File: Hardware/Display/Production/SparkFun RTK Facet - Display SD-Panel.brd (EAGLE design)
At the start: 119.6 x 193.8 mm, 662 parts, among them J1 FPC_12_0.5MM_BACKFLIP, J10 MICRO-SD-PUSH-PUSH-EXT-PIN, J11 FPC_12_0.5MM_BACKFLIP, J12 MICRO-SD-PUSH-PUSH-EXT-PIN, J13 FPC_12_0.5MM_BACKFLIP, J14 MICRO-SD-PUSH-PUSH-EXT-PIN, J15 FPC_12_0.5MM_BACKFLIP, J16 MICRO-SD-PUSH-PUSH-EXT-PIN, J17 FPC_12_0.5MM_BACKFLIP, J18 MICRO-SD-PUSH-PUSH-EXT-PIN, J19 FPC_12_0.5MM_BACKFLIP, J2 MICRO-SD-PUSH-PUSH-EXT-PIN, J20 MICRO-SD-PUSH-PUSH-EXT-PIN, J21 FPC_12_0.5MM_BACKFLIP, J22 MICRO-SD-PUSH-PUSH-EXT-PIN, J23 FPC_12_0.5MM_BACKFLIP, J24 MICRO-SD-PUSH-PUSH-EXT-PIN, J25 FPC_12_0.5MM_BACKFLIP, J26 MICRO-SD-PUSH-PUSH-EXT-PIN, J27 FPC_12_0.5MM_BACKFLIP, J28 MICRO-SD-PUSH-PUSH-EXT-PIN, J29 FPC_12_0.5MM_BACKFLIP, J3 FPC_12_0.5MM_BACKFLIP, J30 MICRO-SD-PUSH-PUSH-EXT-PIN, J31 FPC_12_0.5MM_BACKFLIP, J32 MICRO-SD-PUSH-PUSH-EXT-PIN, J4 MICRO-SD-PUSH-PUSH-EXT-PIN, J5 FPC_12_0.5MM_BACKFLIP, J6 MICRO-SD-PUSH-PUSH-EXT-PIN, J7 FPC_12_0.5MM_BACKFLIP, J8 MICRO-SD-PUSH-PUSH-EXT-PIN, J9 FPC_12_0.5MM_BACKFLIP, U1 LIS2DH12, U10 LIS2DH12, U11 LIS2DH12, U12 LIS2DH12, U13 LIS2DH12, U14 LIS2DH12, U15 LIS2DH12, U16 LIS2DH12, U2 LIS2DH12, U3 LIS2DH12, U4 LIS2DH12, U5 LIS2DH12, U6 LIS2DH12, U7 LIS2DH12, U8 LIS2DH12, U9 LIS2DH12

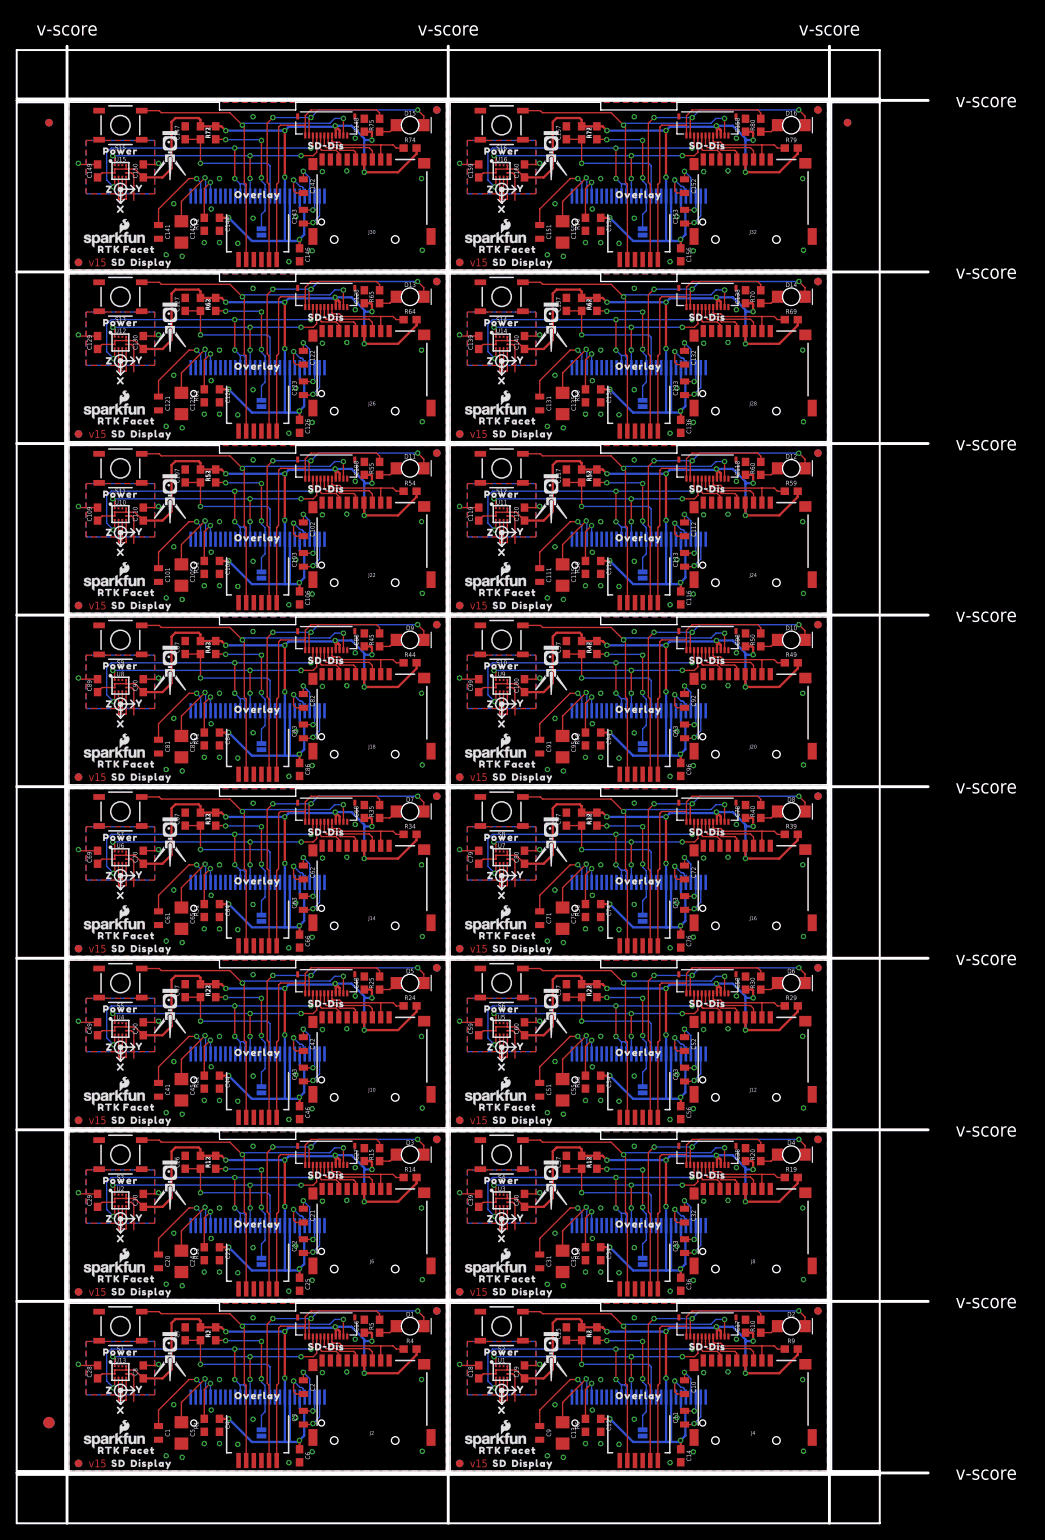
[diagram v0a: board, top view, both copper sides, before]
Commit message: Add I2C test header to display board - v1.6
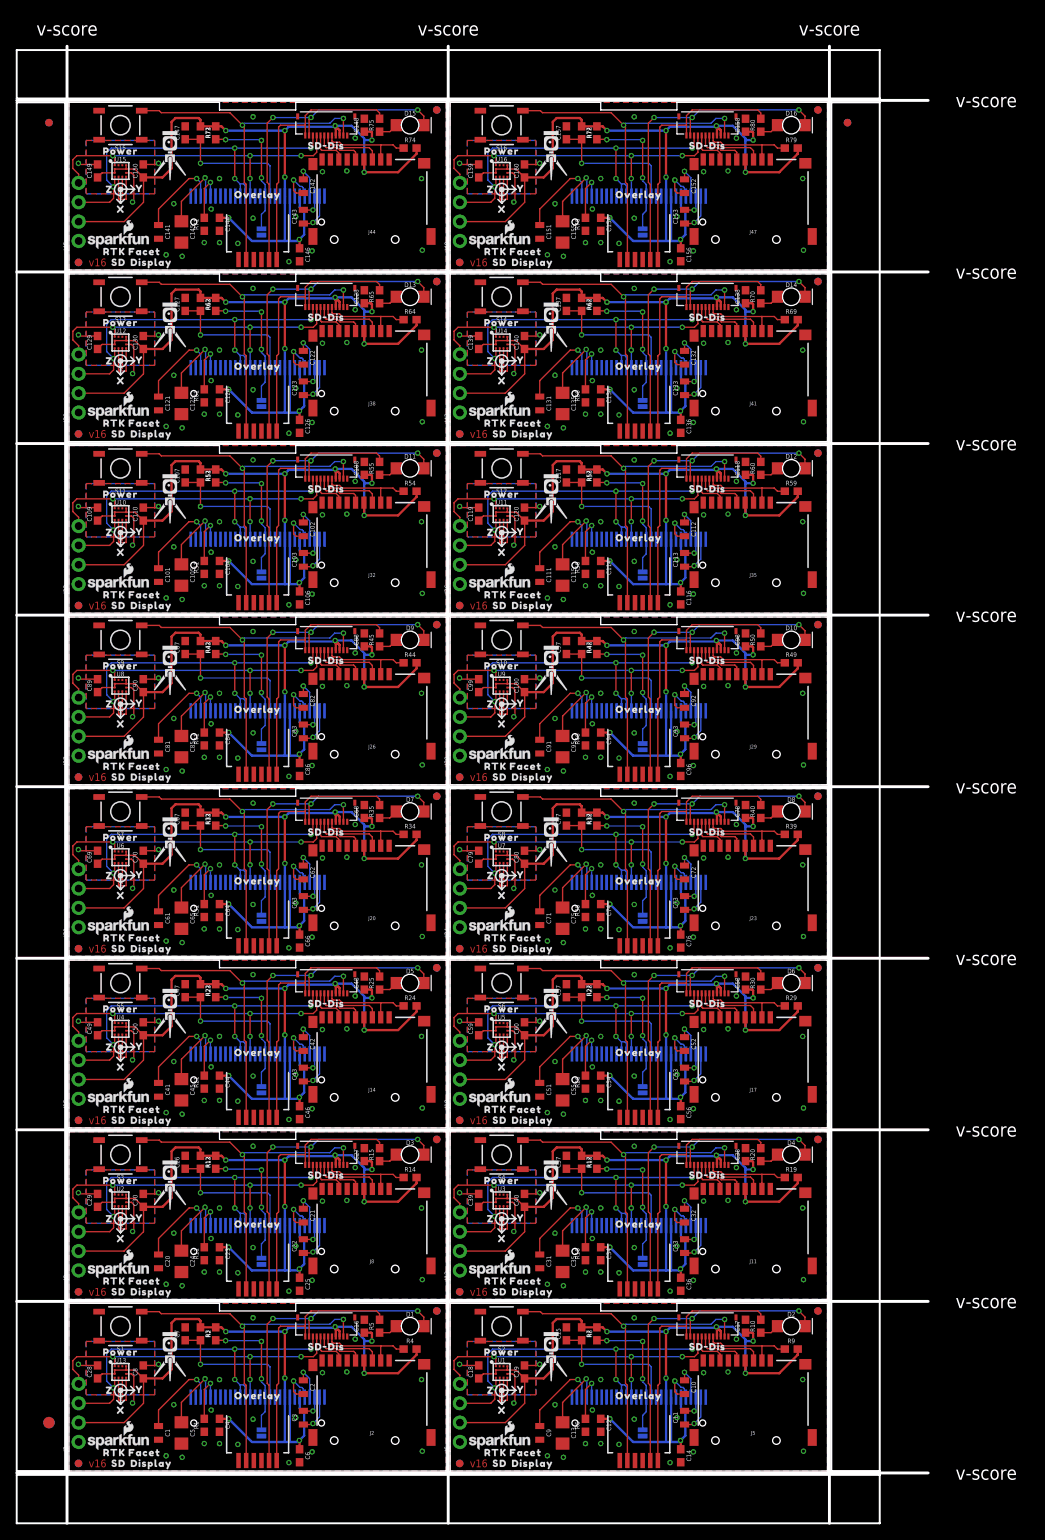
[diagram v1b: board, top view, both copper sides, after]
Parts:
- added J33, J36, J39, J42, J45, J48: (no value), SparkFun-Connectors:1X04_NO_SILK
- added J34, J37, J40, J43, J46: FPC_12_0.5MM_BACKFLIP, RTK Facet:FPC_12_DOUBLESIDED_BACKFLIP
- added J35, J38, J41, J44, J47: MICRO-SD-PUSH-PUSH-EXT-PIN, SparkFun-Connectors:MICROSD-EXTERNALPIN
- added U$193, U$209, U$225, U$241: (no value), output:DISPLAY0
- added U$194, U$210, U$226, U$242: (no value), output:SD1
- added U$195, U$211, U$227, U$243: (no value), output:#ADR#0
- added U$196, U$212, U$228, U$244: (no value), output:SD#DIS0
- added U$197, U$213, U$229, U$245: (no value), output:CHARGE0
- added U$198, U$214, U$230, U$246: (no value), output:OVERLAY0
- added U$199, U$215, U$231, U$247: (no value), output:POWER0
- added U$200, U$216, U$232, U$248: (no value), output:X0
- added U$201, U$217, U$233, U$249: (no value), output:Y1
- added U$202, U$218, U$234, U$250: (no value), output:Z2
- added U$203, U$219, U$235, U$251: (no value), output:RTK_FACET0
- added U$204, U$220, U$236, U$252: (no value), output:RTK5#SVG0
- added U$205, U$221, U$237, U$253: (no value), output:3V33
- added U$206, U$222, U$238, U$254: (no value), output:GND2
- added U$207, U$223, U$239, U$255: (no value), output:SCL0
- added U$208, U$224, U$240, U$256: (no value), output:SDA1
- J10, J16, J22, J28, J4: value MICRO-SD-PUSH-PUSH-EXT-PIN -> FPC_12_0.5MM_BACKFLIP; device SparkFun-Connectors:MICROSD-EXTERNALPIN -> RTK Facet:FPC_12_DOUBLESIDED_BACKFLIP
- J11, J17, J23, J29, J5: value FPC_12_0.5MM_BACKFLIP -> MICRO-SD-PUSH-PUSH-EXT-PIN; device RTK Facet:FPC_12_DOUBLESIDED_BACKFLIP -> SparkFun-Connectors:MICROSD-EXTERNALPIN
- J12, J18, J24, J30, J6: value MICRO-SD-PUSH-PUSH-EXT-PIN -> (none); device SparkFun-Connectors:MICROSD-EXTERNALPIN -> SparkFun-Connectors:1X04_NO_SILK
- J15, J21, J27, J3, J9: value FPC_12_0.5MM_BACKFLIP -> (none); device RTK Facet:FPC_12_DOUBLESIDED_BACKFLIP -> SparkFun-Connectors:1X04_NO_SILK
- U$109, U$157, U$61: device output:DISPLAY0 -> output:3V33
- U$110, U$158, U$62: device output:SD1 -> output:GND2
- U$111, U$159, U$63: device output:#ADR#0 -> output:SCL0
- U$112, U$160, U$64: device output:SD#DIS0 -> output:SDA1
- U$113, U$161, U$65: device output:CHARGE0 -> output:DISPLAY0
- U$114, U$162, U$18, U$66: device output:OVERLAY0 -> output:SD1
- U$115, U$163, U$19, U$67: device output:POWER0 -> output:#ADR#0
- U$116, U$164, U$20, U$68: device output:X0 -> output:SD#DIS0
- U$117, U$165, U$21, U$69: device output:Y1 -> output:CHARGE0
- U$118, U$166, U$22, U$70: device output:Z2 -> output:OVERLAY0
- U$119, U$167, U$23, U$71: device output:RTK_FACET0 -> output:POWER0
- U$120, U$168, U$24, U$72: device output:RTK5#SVG0 -> output:X0
- U$121, U$169, U$25, U$73: device output:DISPLAY0 -> output:Y1
- U$122, U$170, U$26, U$74: device output:SD1 -> output:Z2
- U$123, U$171, U$27, U$75: device output:#ADR#0 -> output:RTK_FACET0
- U$124, U$172, U$28, U$76: device output:SD#DIS0 -> output:RTK5#SVG0
- U$125, U$173, U$29, U$77: device output:CHARGE0 -> output:3V33
- U$126, U$174, U$30, U$78: device output:OVERLAY0 -> output:GND2
- U$127, U$175, U$31, U$79: device output:POWER0 -> output:SCL0
- U$128, U$176, U$32, U$80: device output:X0 -> output:SDA1
- U$129, U$177, U$33, U$81: device output:Y1 -> output:DISPLAY0
- U$130, U$178, U$34, U$82: device output:Z2 -> output:SD1
- U$131, U$179, U$35, U$83: device output:RTK_FACET0 -> output:#ADR#0
- U$132, U$180, U$36, U$84: device output:RTK5#SVG0 -> output:SD#DIS0
- U$133, U$181, U$37, U$85: device output:DISPLAY0 -> output:CHARGE0
- U$134, U$182, U$38, U$86: device output:SD1 -> output:OVERLAY0
- U$135, U$183, U$39, U$87: device output:#ADR#0 -> output:POWER0
- U$136, U$184, U$40, U$88: device output:SD#DIS0 -> output:X0
- U$137, U$185, U$41, U$89: device output:CHARGE0 -> output:Y1
- U$138, U$186, U$42, U$90: device output:OVERLAY0 -> output:Z2
- U$139, U$187, U$43, U$91: device output:POWER0 -> output:RTK_FACET0
- U$14: device output:SD1 -> output:3V33
- U$140, U$188, U$44, U$92: device output:X0 -> output:RTK5#SVG0
- U$141, U$189, U$45, U$93: device output:Y1 -> output:3V33
- U$142, U$190, U$46, U$94: device output:Z2 -> output:GND2
- U$143, U$191, U$47, U$95: device output:RTK_FACET0 -> output:SCL0
- U$144, U$192, U$48, U$96: device output:RTK5#SVG0 -> output:SDA1
- U$15: device output:#ADR#0 -> output:GND2
- U$16: device output:SD#DIS0 -> output:SCL0
- U$17: device output:CHARGE0 -> output:SDA1
- moved J27 102.1 mm to (1.27, 93.8), turned to 90 degrees
- moved J29 99.7 mm to (89.8, 94.0), turned to 0 degrees
- moved U$161 92.4 mm to (10.8, 113.5), flipped to the top
- moved U$17 91.3 mm to (3.81, 8.89)
- moved J15 90.7 mm to (1.27, 48.8), turned to 90 degrees
- moved U$137 90.2 mm to (9.25, 100.7), flipped to the top
- moved U$41 85.7 mm to (9.25, 33.2), flipped to the top
- moved U$65 85.5 mm to (10.8, 46.0), flipped to the top
- moved U$112 85.4 mm to (3.81, 76.4), flipped to the bottom
- moved J3 83.9 mm to (1.27, 3.81), turned to 90 degrees
- moved U$136 83.0 mm to (6.65, 98.0), turned to 180 degrees
- moved U$180 83.0 mm to (83.8, 128.8)
- moved U$179 82.6 mm to (78.3, 117.5), flipped to the bottom
- moved J17 82.1 mm to (89.8, 49.0), turned to 0 degrees
- moved U$16 80.1 mm to (3.81, 11.4), flipped to the bottom
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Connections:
- net 3.3V: now also J3.2
- net 3.3V1: now also J4.3, J5.4, J6.2; no longer J3.3, J3.4
- net 3.3V10: now also J31.3, J31.4, J32.4, J33.2; no longer J21.3, J21.4, J22.4
- net 3.3V11: now also J34.3, J34.4, J35.4, J36.2; no longer J23.3, J23.4, J24.4
- net 3.3V12: now also J37.3, J37.4, J38.4, J39.2; no longer J25.3, J25.4, J26.4
- net 3.3V13: now also J40.3, J40.4, J41.4, J42.2; no longer J27.3, J27.4, J28.4
- net 3.3V14: now also J43.3, J43.4, J44.4, J45.2; no longer J29.3, J29.4, J30.4
- net 3.3V15: now also J46.3, J46.4, J47.4, J48.2; no longer J31.3, J31.4, J32.4
- net 3.3V2: now also J7.3, J7.4, J8.4, J9.2; no longer J5.3, J5.4, J6.4
- net 3.3V3: now also J10.3, J10.4, J11.4, J12.2; no longer J7.3, J7.4, J8.4
- net 3.3V4: now also J13.3, J13.4, J14.4, J15.2; no longer J10.4, J9.3, J9.4
- net 3.3V5: now also J16.3, J16.4, J17.4, J18.2; no longer J11.3, J11.4, J12.4
- net 3.3V6: now also J19.3, J19.4, J20.4, J21.2; no longer J13.3, J13.4, J14.4
- net 3.3V7: now also J22.3, J22.4, J23.4, J24.2; no longer J15.3, J15.4, J16.4
- net 3.3V8: now also J25.3, J25.4, J26.4, J27.2; no longer J17.3, J17.4, J18.4
- net 3.3V9: now also J28.3, J28.4, J29.4, J30.2; no longer J19.3, J19.4, J20.4
- net CHARGE_LED1: now also J4.11; no longer J3.11
- net CHARGE_LED10: now also J31.11; no longer J21.11
- net CHARGE_LED11: now also J34.11; no longer J23.11
- net CHARGE_LED12: now also J37.11; no longer J25.11
- net CHARGE_LED13: now also J40.11; no longer J27.11
- net CHARGE_LED14: now also J43.11; no longer J29.11
- net CHARGE_LED15: now also J46.11; no longer J31.11
- net CHARGE_LED2: now also J7.11; no longer J5.11
- net CHARGE_LED3: now also J10.11; no longer J7.11
- net CHARGE_LED4: now also J13.11; no longer J9.11
- net CHARGE_LED5: now also J16.11; no longer J11.11
- net CHARGE_LED6: now also J19.11; no longer J13.11
- net CHARGE_LED7: now also J22.11; no longer J15.11
- net CHARGE_LED8: now also J25.11; no longer J17.11
- net CHARGE_LED9: now also J28.11; no longer J19.11
- net ESP_21/SDA: now also J3.3
- net ESP_21/SDA1: now also J4.10, J6.3; no longer J3.10
- net ESP_21/SDA10: now also J31.10, J33.3; no longer J21.10
- net ESP_21/SDA11: now also J34.10, J36.3; no longer J23.10
- net ESP_21/SDA12: now also J37.10, J39.3; no longer J25.10
- net ESP_21/SDA13: now also J40.10, J42.3; no longer J27.10
- net ESP_21/SDA14: now also J43.10, J45.3; no longer J29.10
- net ESP_21/SDA15: now also J46.10, J48.3; no longer J31.10
- net ESP_21/SDA2: now also J7.10, J9.3; no longer J5.10
- net ESP_21/SDA3: now also J10.10, J12.3; no longer J7.10
- net ESP_21/SDA4: now also J13.10, J15.3; no longer J9.10
- net ESP_21/SDA5: now also J16.10, J18.3; no longer J11.10
- net ESP_21/SDA6: now also J19.10, J21.3; no longer J13.10
- net ESP_21/SDA7: now also J22.10, J24.3; no longer J15.10
- net ESP_21/SDA8: now also J25.10, J27.3; no longer J17.10
- net ESP_21/SDA9: now also J28.10, J30.3; no longer J19.10
- net ESP_22/SCL: now also J3.4
- net ESP_22/SCL1: now also J4.9, J6.4; no longer J3.9
- net ESP_22/SCL10: now also J31.9, J33.4; no longer J21.9
- net ESP_22/SCL11: now also J34.9, J36.4; no longer J23.9
- net ESP_22/SCL12: now also J37.9, J39.4; no longer J25.9
- net ESP_22/SCL13: now also J40.9, J42.4; no longer J27.9
- net ESP_22/SCL14: now also J43.9, J45.4; no longer J29.9
- net ESP_22/SCL15: now also J46.9, J48.4; no longer J31.9
- net ESP_22/SCL2: now also J7.9, J9.4; no longer J5.9
- net ESP_22/SCL3: now also J10.9, J12.4; no longer J7.9
- net ESP_22/SCL4: now also J13.9, J15.4; no longer J9.9
- net ESP_22/SCL5: now also J16.9, J18.4; no longer J11.9
- net ESP_22/SCL6: now also J19.9, J21.4; no longer J13.9
- net ESP_22/SCL7: now also J22.9, J24.4; no longer J15.9
- net ESP_22/SCL8: now also J25.9, J27.4; no longer J17.9
- net ESP_22/SCL9: now also J28.9, J30.4; no longer J19.9
- net GND: now also J3.1
- net GND1: now also J4.1, J5.10, J5.11, J5.12, J5.13, J5.6, J5.9, J6.1; no longer J3.1, J4.10, J4.11, J4.12, J4.13, J4.6, J4.9
- net GND10: now also J31.1, J32.10, J32.11, J32.12, J32.13, J32.6, J32.9, J33.1; no longer J21.1, J22.10, J22.11, J22.12, J22.13, J22.6, J22.9
- net GND11: now also J34.1, J35.10, J35.11, J35.12, J35.13, J35.6, J35.9, J36.1; no longer J23.1, J24.10, J24.11, J24.12, J24.13, J24.6, J24.9
- net GND12: now also J37.1, J38.10, J38.11, J38.12, J38.13, J38.6, J38.9, J39.1; no longer J25.1, J26.10, J26.11, J26.12, J26.13, J26.6, J26.9
- net GND13: now also J40.1, J41.10, J41.11, J41.12, J41.13, J41.6, J41.9, J42.1; no longer J27.1, J28.10, J28.11, J28.12, J28.13, J28.6, J28.9
- net GND14: now also J43.1, J44.10, J44.11, J44.12, J44.13, J44.6, J44.9, J45.1; no longer J29.1, J30.10, J30.11, J30.12, J30.13, J30.6, J30.9
- net GND15: now also J46.1, J47.10, J47.11, J47.12, J47.13, J47.6, J47.9, J48.1; no longer J31.1, J32.10, J32.11, J32.12, J32.13, J32.6, J32.9
- net GND2: now also J7.1, J8.10, J8.11, J8.12, J8.13, J8.6, J8.9, J9.1; no longer J5.1, J6.10, J6.11, J6.12, J6.13, J6.6, J6.9
- net GND3: now also J10.1, J11.10, J11.11, J11.12, J11.13, J11.6, J11.9, J12.1; no longer J7.1, J8.10, J8.11, J8.12, J8.13, J8.6, J8.9
- net GND4: now also J13.1, J14.10, J14.11, J14.12, J14.13, J14.6, J14.9, J15.1; no longer J10.10, J10.11, J10.12, J10.13, J10.6, J10.9, J9.1
- net GND5: now also J16.1, J17.10, J17.11, J17.12, J17.13, J17.6, J17.9, J18.1; no longer J11.1, J12.10, J12.11, J12.12, J12.13, J12.6, J12.9
- net GND6: now also J19.1, J20.10, J20.11, J20.12, J20.13, J20.6, J20.9, J21.1; no longer J13.1, J14.10, J14.11, J14.12, J14.13, J14.6, J14.9
- net GND7: now also J22.1, J23.10, J23.11, J23.12, J23.13, J23.6, J23.9, J24.1; no longer J15.1, J16.10, J16.11, J16.12, J16.13, J16.6, J16.9
- net GND8: now also J25.1, J26.10, J26.11, J26.12, J26.13, J26.6, J26.9, J27.1; no longer J17.1, J18.10, J18.11, J18.12, J18.13, J18.6, J18.9
- net GND9: now also J28.1, J29.10, J29.11, J29.12, J29.13, J29.6, J29.9, J30.1; no longer J19.1, J20.10, J20.11, J20.12, J20.13, J20.6, J20.9
- net POWER_BTN1: now also J4.2; no longer J3.2
- net POWER_BTN10: now also J31.2; no longer J21.2
- net POWER_BTN11: now also J34.2; no longer J23.2
- net POWER_BTN12: now also J37.2; no longer J25.2
- net POWER_BTN13: now also J40.2; no longer J27.2
- net POWER_BTN14: now also J43.2; no longer J29.2
- net POWER_BTN15: now also J46.2; no longer J31.2
- net POWER_BTN2: now also J7.2; no longer J5.2
- net POWER_BTN3: now also J10.2; no longer J7.2
- net POWER_BTN4: now also J13.2; no longer J9.2
- net POWER_BTN5: now also J16.2; no longer J11.2
- net POWER_BTN6: now also J19.2; no longer J13.2
- net POWER_BTN7: now also J22.2; no longer J15.2
- net POWER_BTN8: now also J25.2; no longer J17.2
- net POWER_BTN9: now also J28.2; no longer J19.2
- net SD_!CS!1: now also J4.5, J5.2; no longer J3.5, J4.2
- net SD_!CS!10: now also J31.5, J32.2; no longer J21.5, J22.2
- net SD_!CS!11: now also J34.5, J35.2; no longer J23.5, J24.2
- net SD_!CS!12: now also J37.5, J38.2; no longer J25.5, J26.2
- net SD_!CS!13: now also J40.5, J41.2; no longer J27.5, J28.2
- net SD_!CS!14: now also J43.5, J44.2; no longer J29.5, J30.2
- net SD_!CS!15: now also J46.5, J47.2; no longer J31.5, J32.2
- net SD_!CS!2: now also J7.5, J8.2; no longer J5.5, J6.2
- net SD_!CS!3: now also J10.5, J11.2; no longer J7.5, J8.2
- net SD_!CS!4: now also J13.5, J14.2; no longer J10.2, J9.5
- net SD_!CS!5: now also J16.5, J17.2; no longer J11.5, J12.2
- net SD_!CS!6: now also J19.5, J20.2; no longer J13.5, J14.2
- net SD_!CS!7: now also J22.5, J23.2; no longer J15.5, J16.2
- net SD_!CS!8: now also J25.5, J26.2; no longer J17.5, J18.2
- net SD_!CS!9: now also J28.5, J29.2; no longer J19.5, J20.2
- net SD_CIPO1: now also J4.8, J5.7; no longer J3.8, J4.7
- net SD_CIPO10: now also J31.8, J32.7; no longer J21.8, J22.7
- net SD_CIPO11: now also J34.8, J35.7; no longer J23.8, J24.7
- net SD_CIPO12: now also J37.8, J38.7; no longer J25.8, J26.7
- net SD_CIPO13: now also J40.8, J41.7; no longer J27.8, J28.7
- net SD_CIPO14: now also J43.8, J44.7; no longer J29.8, J30.7
- net SD_CIPO15: now also J46.8, J47.7; no longer J31.8, J32.7
- net SD_CIPO2: now also J7.8, J8.7; no longer J5.8, J6.7
- net SD_CIPO3: now also J10.8, J11.7; no longer J7.8, J8.7
- net SD_CIPO4: now also J13.8, J14.7; no longer J10.7, J9.8
- net SD_CIPO5: now also J16.8, J17.7; no longer J11.8, J12.7
- net SD_CIPO6: now also J19.8, J20.7; no longer J13.8, J14.7
- net SD_CIPO7: now also J22.8, J23.7; no longer J15.8, J16.7
- net SD_CIPO8: now also J25.8, J26.7; no longer J17.8, J18.7
- net SD_CIPO9: now also J28.8, J29.7; no longer J19.8, J20.7
- net SD_COPI1: now also J4.6, J5.3; no longer J3.6, J4.3
- net SD_COPI10: now also J31.6, J32.3; no longer J21.6, J22.3
- net SD_COPI11: now also J34.6, J35.3; no longer J23.6, J24.3
- net SD_COPI12: now also J37.6, J38.3; no longer J25.6, J26.3
- net SD_COPI13: now also J40.6, J41.3; no longer J27.6, J28.3
- net SD_COPI14: now also J43.6, J44.3; no longer J29.6, J30.3
- net SD_COPI15: now also J46.6, J47.3; no longer J31.6, J32.3
- net SD_COPI2: now also J7.6, J8.3; no longer J5.6, J6.3
- net SD_COPI3: now also J10.6, J11.3; no longer J7.6, J8.3
- net SD_COPI4: now also J13.6, J14.3; no longer J10.3, J9.6
- net SD_COPI5: now also J16.6, J17.3; no longer J11.6, J12.3
- net SD_COPI6: now also J19.6, J20.3; no longer J13.6, J14.3
- net SD_COPI7: now also J22.6, J23.3; no longer J15.6, J16.3
- net SD_COPI8: now also J25.6, J26.3; no longer J17.6, J18.3
- net SD_COPI9: now also J28.6, J29.3; no longer J19.6, J20.3
- net SD_SCK1: now also J4.7, J5.5; no longer J3.7, J4.5
- net SD_SCK10: now also J31.7, J32.5; no longer J21.7, J22.5
- net SD_SCK11: now also J34.7, J35.5; no longer J23.7, J24.5
- net SD_SCK12: now also J37.7, J38.5; no longer J25.7, J26.5
- net SD_SCK13: now also J40.7, J41.5; no longer J27.7, J28.5
- net SD_SCK14: now also J43.7, J44.5; no longer J29.7, J30.5
- net SD_SCK15: now also J46.7, J47.5; no longer J31.7, J32.5
- net SD_SCK2: now also J7.7, J8.5; no longer J5.7, J6.5
- net SD_SCK3: now also J10.7, J11.5; no longer J7.7, J8.5
- net SD_SCK4: now also J13.7, J14.5; no longer J10.5, J9.7
- net SD_SCK5: now also J16.7, J17.5; no longer J11.7, J12.5
- net SD_SCK6: now also J19.7, J20.5; no longer J13.7, J14.5
- net SD_SCK7: now also J22.7, J23.5; no longer J15.7, J16.5
- net SD_SCK8: now also J25.7, J26.5; no longer J17.7, J18.5
- net SD_SCK9: now also J28.7, J29.5; no longer J19.7, J20.5
- net V_USB1: now also J4.12; no longer J3.12
- net V_USB10: now also J31.12; no longer J21.12
- net V_USB11: now also J34.12; no longer J23.12
- net V_USB12: now also J37.12; no longer J25.12
- net V_USB13: now also J40.12; no longer J27.12
- net V_USB14: now also J43.12; no longer J29.12
- net V_USB15: now also J46.12; no longer J31.12
- net V_USB2: now also J7.12; no longer J5.12
- net V_USB3: now also J10.12; no longer J7.12
- net V_USB4: now also J13.12; no longer J9.12
- net V_USB5: now also J16.12; no longer J11.12
- net V_USB6: now also J19.12; no longer J13.12
- net V_USB7: now also J22.12; no longer J15.12
- net V_USB8: now also J25.12; no longer J17.12
- net V_USB9: now also J28.12; no longer J19.12
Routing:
- net 3.3V9: track 105.6 -> 118.4 mm
- net 3.3V7: track 105.6 -> 118.4 mm
- net 3.3V5: track 105.6 -> 118.4 mm
- net 3.3V4: track 105.6 -> 118.4 mm
- net 3.3V3: track 105.6 -> 118.4 mm
- net 3.3V2: track 105.6 -> 118.4 mm
- net 3.3V11: track 105.6 -> 118.4 mm
- net 3.3V8: track 105.6 -> 118.4 mm
- net 3.3V6: track 105.6 -> 118.4 mm
- net 3.3V15: track 105.6 -> 118.4 mm
- net 3.3V13: track 105.6 -> 118.4 mm
- net 3.3V10: track 105.6 -> 118.4 mm
- net 3.3V1: track 105.6 -> 118.4 mm
- net 3.3V: track 105.6 -> 118.4 mm
- net 3.3V14: track 105.6 -> 118.4 mm
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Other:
- board text added: "v16"
- board text removed: "v15"

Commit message: Remove silk from around the accel FP for DFM.
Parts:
- JP11, JP13, JP15, JP17, JP19, JP2, JP21, JP23, JP25, JP27, JP29, JP3, JP31, JP5, JP7, JP9: value (none) -> JUMPER-SMT_2_NO_SILK
- U1, U10, U11, U12, U13, U14, U15, U16, U2, U3, U4, U5, U6, U7, U8, U9: value LIS2DH12 -> LIS2DH12NS; device SparkFun-Sensors:LGA-12-LISDH12 -> SparkFun-Sensors:LGA-12-LISDH12-NOSILK
- moved U$105 12.0 mm to (20.7, 82.0)
- moved U$11 12.0 mm to (20.7, 14.5)
- moved U$120 12.0 mm to (68.1, 79.3)
- moved U$137 12.0 mm to (20.7, 104.5)
- moved U$154 12.0 mm to (66.6, 104.4)
- moved U$169 12.0 mm to (20.7, 127.0)
- moved U$184 12.0 mm to (68.1, 124.3)
- moved U$186 12.0 mm to (66.6, 126.9)
- moved U$201 12.0 mm to (20.7, 149.6)
- moved U$216 12.0 mm to (68.1, 146.9)
- moved U$233 12.0 mm to (20.7, 172.1)
- moved U$24 12.0 mm to (68.1, 11.8)
- moved U$248 12.0 mm to (68.1, 169.4)
- moved U$26 12.0 mm to (66.6, 14.4)
- moved U$56 12.0 mm to (68.1, 34.3)
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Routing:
- net N$79: track 0.00 -> 1.22 mm
- net N$69: track 0.00 -> 1.22 mm
- net N$74: track 0.00 -> 1.22 mm
- net N$64: track 0.00 -> 1.22 mm
- net N$39: track 0.00 -> 1.22 mm
- net N$19: track 0.00 -> 1.22 mm
- net N$34: track 0.00 -> 1.22 mm
- net N$14: track 0.00 -> 1.22 mm
- net N$9: track 0.00 -> 1.22 mm
- net N$29: track 0.00 -> 1.22 mm
- net N$4: track 0.00 -> 1.22 mm
- net N$24: track 0.00 -> 1.22 mm
- net N$59: track 0.00 -> 1.22 mm
- net N$49: track 0.00 -> 1.22 mm
- net N$54: track 0.00 -> 1.22 mm
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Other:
- board text added: "v17"
- board text removed: "v16"
